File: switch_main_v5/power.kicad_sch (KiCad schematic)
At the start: 0 parts

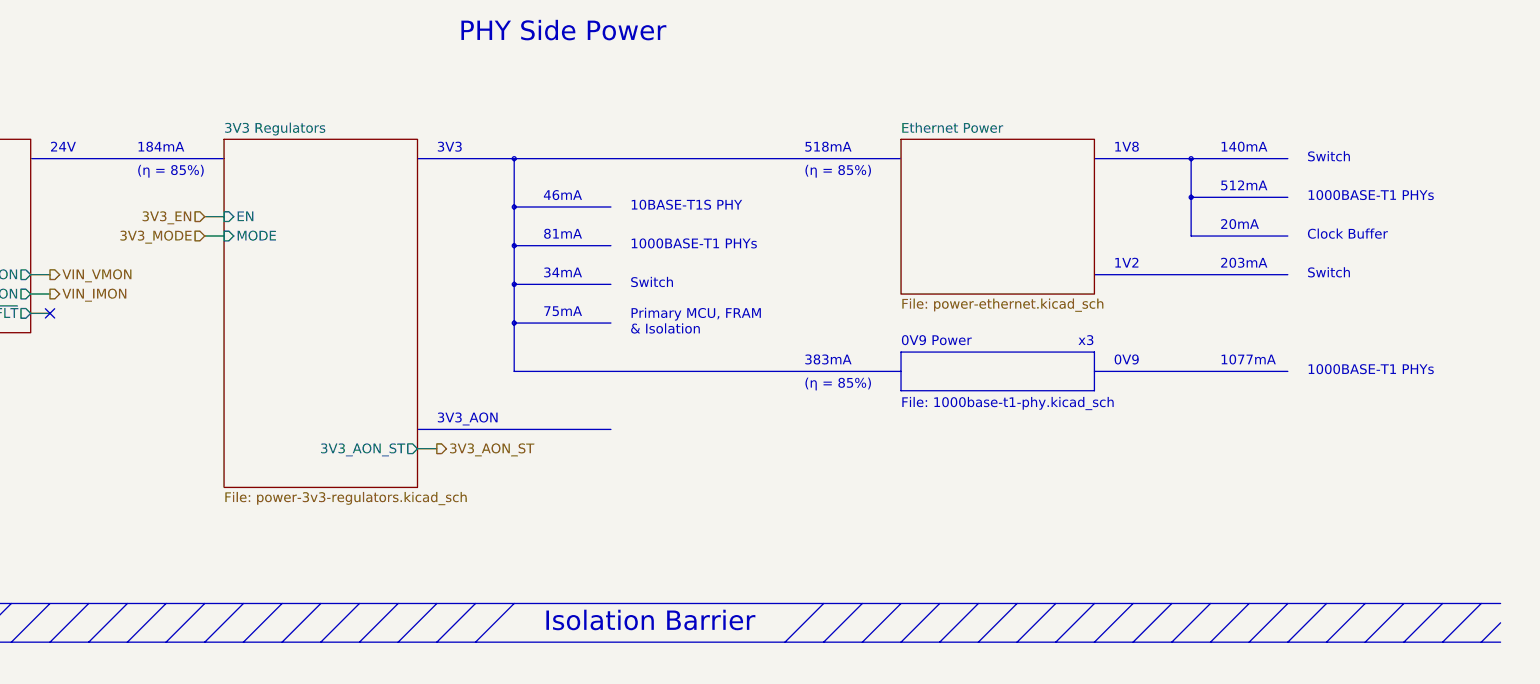
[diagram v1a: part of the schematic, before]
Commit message: Started updating regulators for v5
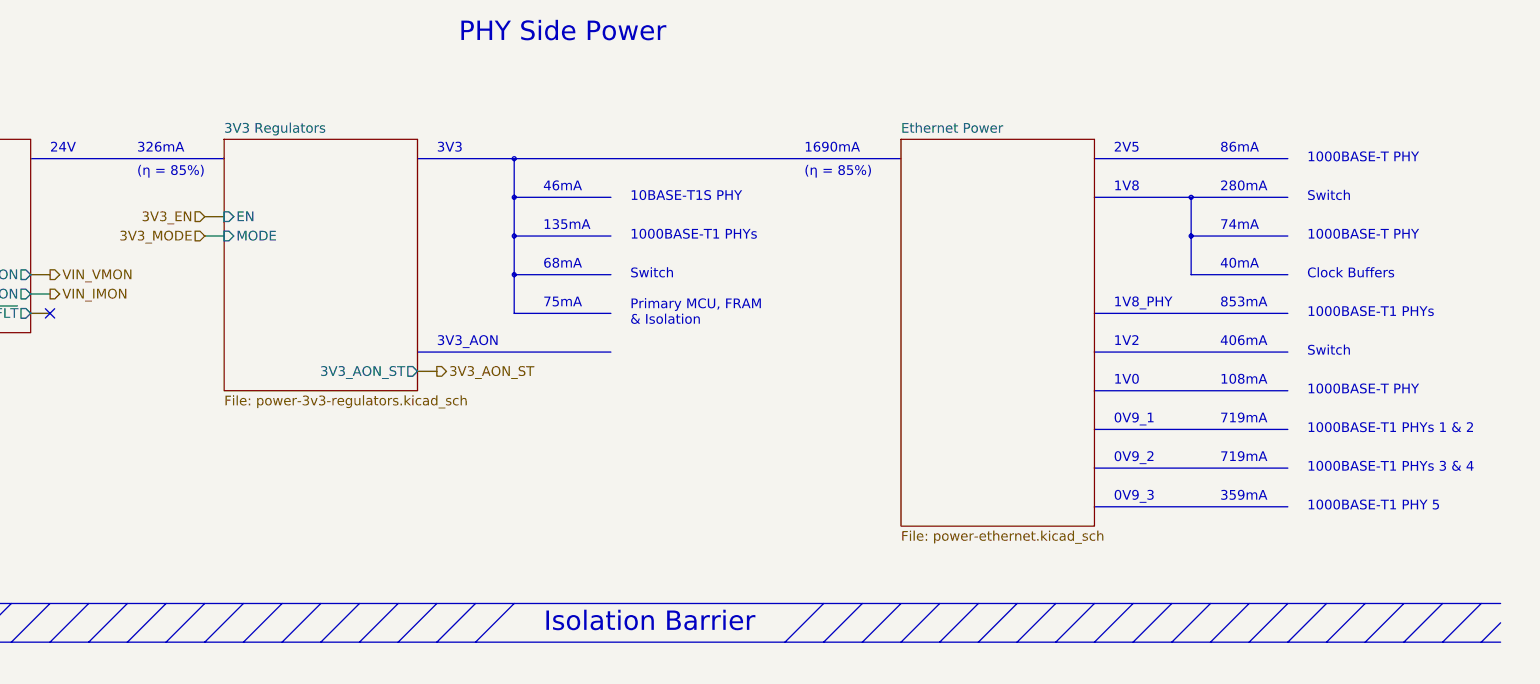
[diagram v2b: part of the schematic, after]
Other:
- note added: "0V9_1"
- note added: "0V9_2"
- note added: "0V9_3"
- note added: "1000BASE-T PHY"
- note added: "1000BASE-T1 PHY 5"
- note added: "1000BASE-T1 PHYs 1 & 2"
- note added: "1000BASE-T1 PHYs 3 & 4"
- note added: "108mA"
- note added: "135mA"
- note added: "1690mA"
- note added: "1V0"
- note added: "1V8_PHY"
- note added: "280mA"
- note added: "2V5"
- note added: "326mA"
- note added: "359mA"
- note added: "406mA"
- note added: "68mA"
- note added: "719mA"
- note added: "74mA"
- note added: "853mA"
- note added: "86mA"
- note added: "Clock Buffers"
- note removed: "0V9"
- note removed: "0V9 Power"
- note removed: "1077mA"
- note removed: "140mA"
- note removed: "184mA"
- note removed: "203mA"
- note removed: "20mA"
- note removed: "34mA"
- note removed: "383mA"
- note removed: "512mA"
- note removed: "518mA"
- note removed: "81mA"
- note removed: "Clock Buffer"
- note removed: "File: 1000base-t1-phy.kicad_sch"
- note removed: "x3"

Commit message: Placed 1000BASE-T PHY decoupling capacitors
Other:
- note added: "Switches"
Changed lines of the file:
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@@
 		)
 	)
-	(text "Switch"
+	(text "Switches"
 		(exclude_from_sim no)
 		(at 243.84 48.26 0)
@@
 		)
 	)
-	(text "Switch"
+	(text "Switches"
 		(exclude_from_sim no)
 		(at 243.84 68.58 0)
